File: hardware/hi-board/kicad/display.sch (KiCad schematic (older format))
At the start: 2 parts, among them U2 ER-TFT040-2

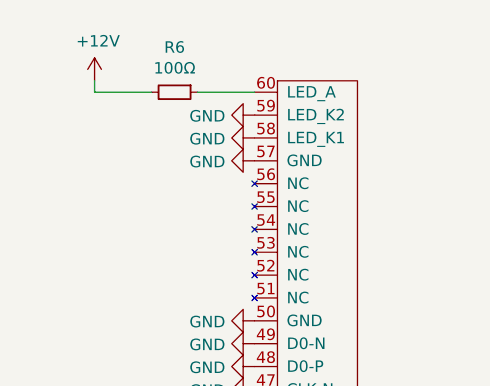
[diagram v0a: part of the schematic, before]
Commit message: Add potentiometer to display schematic
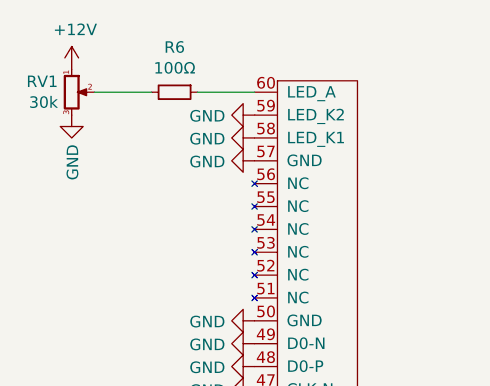
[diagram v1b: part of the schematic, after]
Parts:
- added RV1: 30k, symbol Device:R_POT_Small
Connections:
- net +12V: now also RV1.1; no longer R6.2
- net GND: now also RV1.3
- new net: R6.2, RV1.2
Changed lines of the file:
@@
 Wire Wire Line
 	5750 950  6000 950
-Wire Wire Line
-	5550 950  5300 950
-Wire Wire Line
-	5300 950  5300 900
 $Comp
 L power:+12V #PWR0128
 U 1 1 61427A96
-P 5300 900
-F 0 "#PWR0128" H 5300 750 50  0001 C CNN
-F 1 "+12V" H 5315 1073 50  0000 C CNN
-F 2 "" H 5300 900 50  0001 C CNN
-F 3 "" H 5300 900 50  0001 C CNN
-	1    5300 900
+P 5200 850
+F 0 "#PWR0128" H 5200 700 50  0001 C CNN
+F 1 "+12V" H 5215 1023 50  0000 C CNN
+F 2 "" H 5200 850 50  0001 C CNN
+F 3 "" H 5200 850 50  0001 C CNN
+	1    5200 850
 	1    0    0    -1
 $EndComp
@@
 	0    -1   -1   0
 $EndComp
+$Comp
+L Device:R_POT_Small RV1
+U 1 1 6144926C
+P 5200 950
+F 0 "RV1" H 5140 996 50  0000 R CNN
+F 1 "30k" H 5140 905 50  0000 R CNN
+F 2 "" H 5200 950 50  0001 C CNN
+F 3 "~" H 5200 950 50  0001 C CNN
+	1    5200 950
+	1    0    0    -1
+$EndComp
+$Comp
+L power:GND #PWR0164
+U 1 1 6144A423
+P 5200 1050
+F 0 "#PWR0164" H 5200 800 50  0001 C CNN
+F 1 "GND" V 5205 922 50  0000 R CNN
+F 2 "" H 5200 1050 50  0001 C CNN
+F 3 "" H 5200 1050 50  0001 C CNN
+	1    5200 1050
+	1    0    0    -1
+$EndComp
+Wire Wire Line
+	5300 950  5550 950
 $EndSCHEMATC

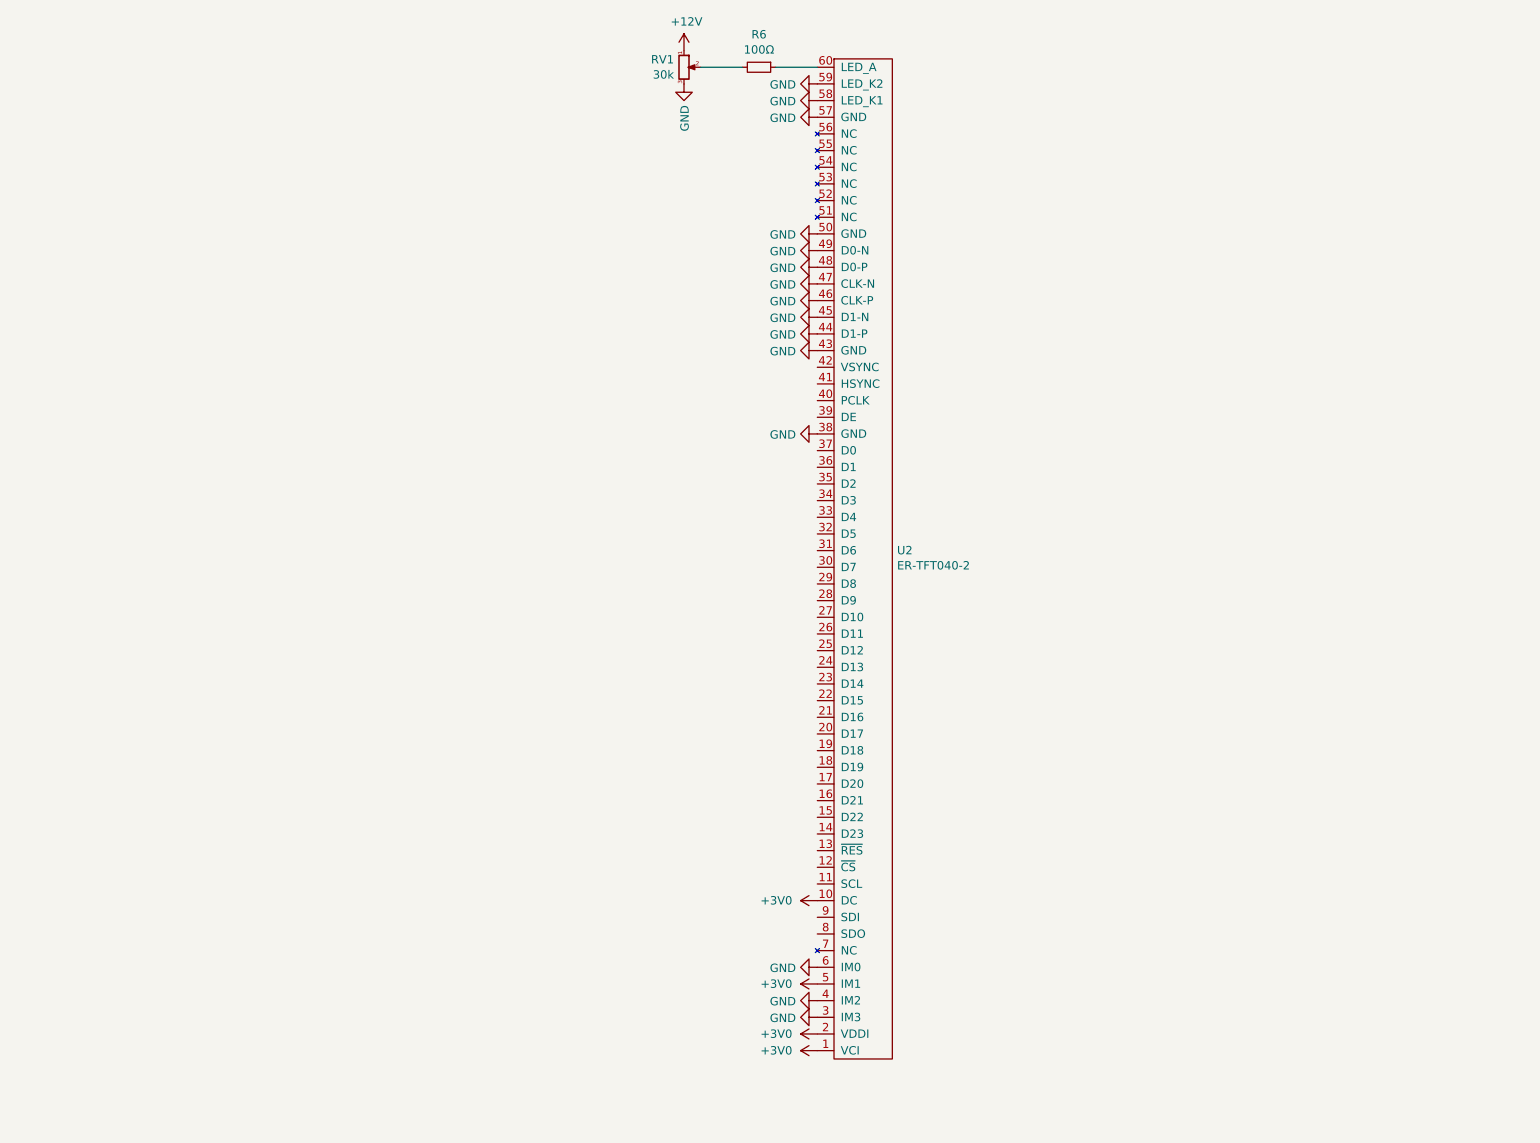
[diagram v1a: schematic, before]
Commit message: Add level shifters
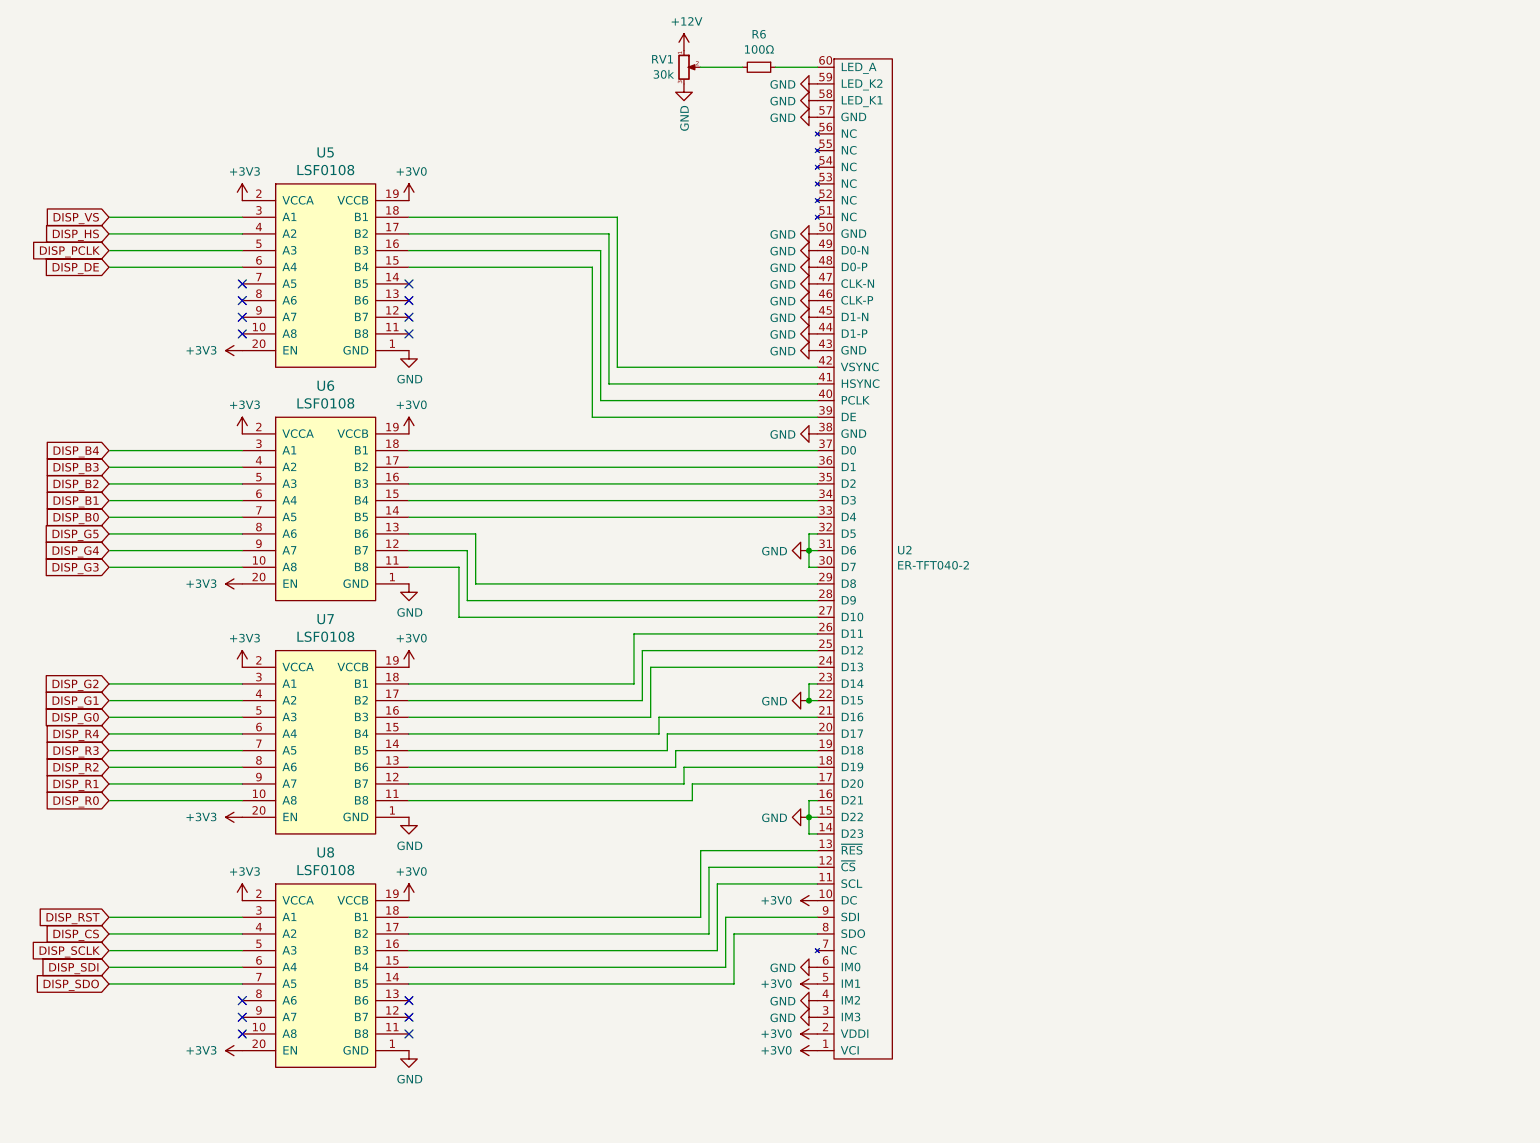
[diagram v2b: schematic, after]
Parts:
- added U5, U6, U7, U8: LSF0108, Package_SO:TSSOP-20_4.4x6.5mm_P0.65mm, symbol hi-board:LSF0108
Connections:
- net +3V0: now also U5.19 (VCCB), U6.19 (VCCB), U7.19 (VCCB), U8.19 (VCCB)
- net GND: now also U2.14 (D23), U2.15 (D22), U2.16 (D21), U2.22 (D15), U2.23 (D14), U2.30 (D7), U2.31 (D6), U2.32 (D5), U5.1 (GND), U6.1 (GND), U7.1 (GND), U8.1 (GND)
- net at U2.11 (SCL): now also U8.16 (B3)
- net at U2.12 (~CS): now also U8.17 (B2)
- net at U2.13 (~RES): now also U8.18 (B1)
- net at U2.17 (D20): now also U7.11 (B8)
- net at U2.18 (D19): now also U7.12 (B7)
- net at U2.19 (D18): now also U7.13 (B6)
- net at U2.20 (D17): now also U7.14 (B5)
- net at U2.21 (D16): now also U7.15 (B4)
- net at U2.24 (D13): now also U7.16 (B3)
- net at U2.25 (D12): now also U7.17 (B2)
- net at U2.26 (D11): now also U7.18 (B1)
- net at U2.27 (D10): now also U6.11 (B8)
- net at U2.28 (D9): now also U6.12 (B7)
- net at U2.29 (D8): now also U6.13 (B6)
- net at U2.33 (D4): now also U6.14 (B5)
- net at U2.34 (D3): now also U6.15 (B4)
- net at U2.35 (D2): now also U6.16 (B3)
- net at U2.36 (D1): now also U6.17 (B2)
- net at U2.37 (D0): now also U6.18 (B1)
- net at U2.39 (DE): now also U5.15 (B4)
- net at U2.40 (PCLK): now also U5.16 (B3)
- net at U2.41 (HSYNC): now also U5.17 (B2)
- net at U2.42 (VSYNC): now also U5.18 (B1)
- net at U2.8 (SDO): now also U8.14 (B5)
- net at U2.9 (SDI): now also U8.15 (B4)
- new net +3V3: U5.2 (VCCA), U5.20 (EN), U6.2 (VCCA), U6.20 (EN), U7.2 (VCCA), U7.20 (EN), U8.2 (VCCA), U8.20 (EN)
- new net DISP_B0: U6.7 (A5)
- new net DISP_B1: U6.6 (A4)
- new net DISP_B2: U6.5 (A3)
- new net DISP_B3: U6.4 (A2)
- new net DISP_B4: U6.3 (A1)
- new net DISP_CS: U8.4 (A2)
- new net DISP_DE: U5.6 (A4)
- new net DISP_G0: U7.5 (A3)
- new net DISP_G1: U7.4 (A2)
- new net DISP_G2: U7.3 (A1)
- new net DISP_G3: U6.10 (A8)
- new net DISP_G4: U6.9 (A7)
- new net DISP_G5: U6.8 (A6)
- new net DISP_HS: U5.4 (A2)
- new net DISP_PCLK: U5.5 (A3)
- new net DISP_R0: U7.10 (A8)
- new net DISP_R1: U7.9 (A7)
- new net DISP_R2: U7.8 (A6)
- new net DISP_R3: U7.7 (A5)
- new net DISP_R4: U7.6 (A4)
- new net DISP_RST: U8.3 (A1)
- new net DISP_SCLK: U8.5 (A3)
- new net DISP_SDI: U8.6 (A4)
- new net DISP_SDO: U8.7 (A5)
- new net DISP_VS: U5.3 (A1)
- no-connect marks 0 -> 14

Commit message: Complete display schematic and change footprints
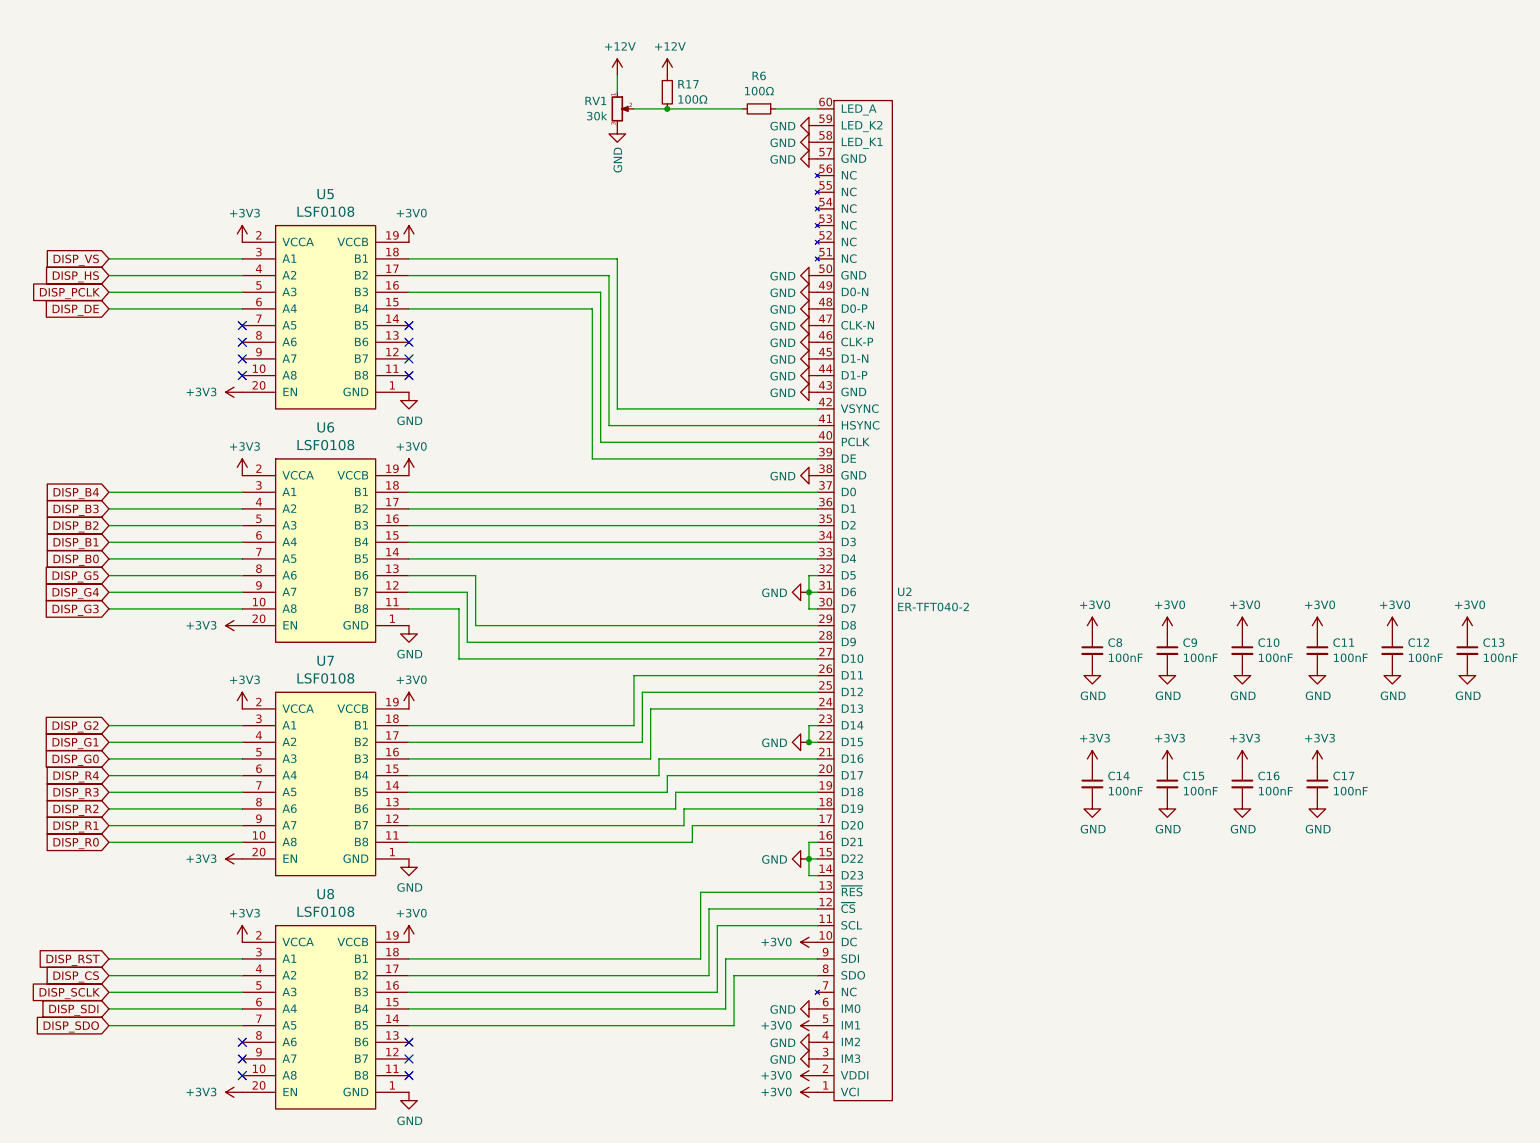
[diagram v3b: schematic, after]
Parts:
- added C10, C11, C12, C13, C14, C15, C16, C17, C8, C9: 100nF, Capacitor_SMD:C_0603_1608Metric, symbol Device:C_Small
- added R17: 100Ω, Resistor_SMD:R_0603_1608Metric, symbol Device:R_Small
- R6: footprint Resistor_SMD:R_0402_1005Metric -> Resistor_SMD:R_0603_1608Metric
- RV1: footprint (none) -> hi-board:Dual_Pot
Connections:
- net +12V: now also R17.1
- net +3V0: now also C10.1, C11.1, C12.1, C13.1, C8.1, C9.1
- net +3V3: now also C14.1, C15.1, C16.1, C17.1
- net GND: now also C10.2, C11.2, C12.2, C13.2, C14.2, C15.2, C16.2, C17.2, C8.2, C9.2
- net at R6.2, RV1.2: now also R17.2
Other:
- moved on the sheet: R6, RV1, U2, U5, U6, U7, U8

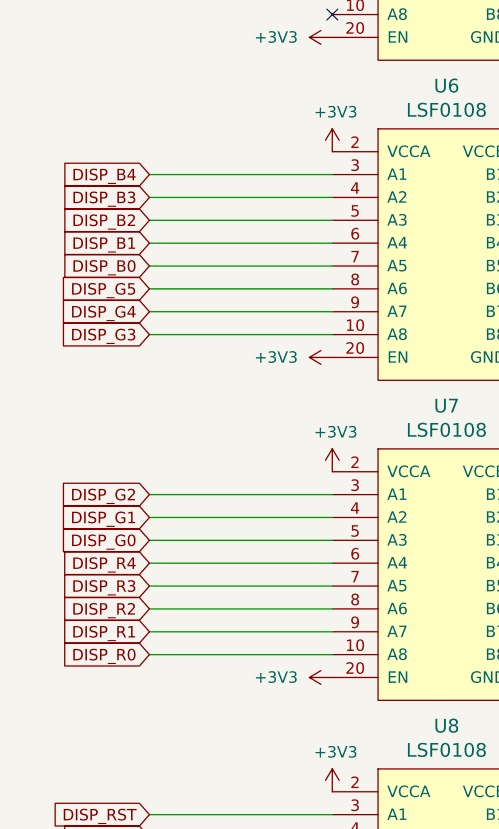
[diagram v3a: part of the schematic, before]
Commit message: Place connector components
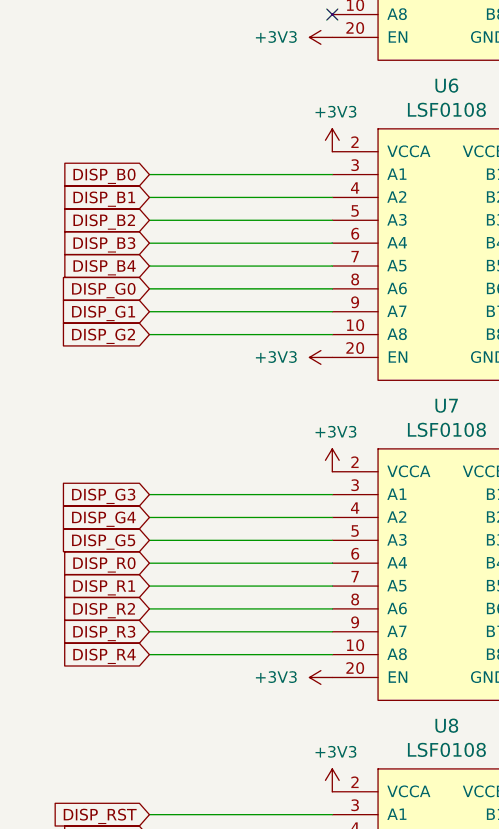
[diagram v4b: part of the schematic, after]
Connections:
- net DISP_B0: now also U6.3 (A1); no longer U6.7 (A5)
- net DISP_B1: now also U6.4 (A2); no longer U6.6 (A4)
- net DISP_B3: now also U6.6 (A4); no longer U6.4 (A2)
- net DISP_B4: now also U6.7 (A5); no longer U6.3 (A1)
- net DISP_G0: now also U6.8 (A6); no longer U7.5 (A3)
- net DISP_G1: now also U6.9 (A7); no longer U7.4 (A2)
- net DISP_G2: now also U6.10 (A8); no longer U7.3 (A1)
- net DISP_G3: now also U7.3 (A1); no longer U6.10 (A8)
- net DISP_G4: now also U7.4 (A2); no longer U6.9 (A7)
- net DISP_G5: now also U7.5 (A3); no longer U6.8 (A6)
- net DISP_R0: now also U7.6 (A4); no longer U7.10 (A8)
- net DISP_R1: now also U7.7 (A5); no longer U7.9 (A7)
- net DISP_R3: now also U7.9 (A7); no longer U7.7 (A5)
- net DISP_R4: now also U7.10 (A8); no longer U7.6 (A4)
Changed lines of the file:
@@
 Wire Wire Line
 	1750 3500 2550 3500
-Text GLabel 1750 5600 0    50   Input ~ 0
+Text GLabel 1750 5200 0    50   Input ~ 0
 DISP_R0
 Wire Wire Line
 	1750 5600 2550 5600
-Text GLabel 1750 5500 0    50   Input ~ 0
+Text GLabel 1750 5300 0    50   Input ~ 0
 DISP_R1
 Text GLabel 1750 5400 0    50   Input ~ 0
 DISP_R2
-Text GLabel 1750 5300 0    50   Input ~ 0
+Text GLabel 1750 5500 0    50   Input ~ 0
 DISP_R3
-Text GLabel 1750 5200 0    50   Input ~ 0
+Text GLabel 1750 5600 0    50   Input ~ 0
 DISP_R4
-Text GLabel 1750 5100 0    50   Input ~ 0
+Text GLabel 1750 4000 0    50   Input ~ 0
 DISP_G0
-Text GLabel 1750 5000 0    50   Input ~ 0
+Text GLabel 1750 4100 0    50   Input ~ 0
 DISP_G1
-Text GLabel 1750 4900 0    50   Input ~ 0
+Text GLabel 1750 4200 0    50   Input ~ 0
 DISP_G2
 Wire Wire Line
@@
 Wire Wire Line
 	3950 4000 3550 4000
-Text GLabel 1750 4200 0    50   Input ~ 0
+Text GLabel 1750 4900 0    50   Input ~ 0
 DISP_G3
 Wire Wire Line
 	1750 4200 2550 4200
-Text GLabel 1750 4100 0    50   Input ~ 0
+Text GLabel 1750 5000 0    50   Input ~ 0
 DISP_G4
-Text GLabel 1750 4000 0    50   Input ~ 0
+Text GLabel 1750 5100 0    50   Input ~ 0
 DISP_G5
 Wire Wire Line
@@
 Wire Wire Line
 	3550 3600 6000 3600
-Text GLabel 1750 3900 0    50   Input ~ 0
+Text GLabel 1750 3500 0    50   Input ~ 0
 DISP_B0
 Wire Wire Line
 	1750 3900 2550 3900
-Text GLabel 1750 3800 0    50   Input ~ 0
+Text GLabel 1750 3600 0    50   Input ~ 0
 DISP_B1
 Text GLabel 1750 3700 0    50   Input ~ 0
 DISP_B2
-Text GLabel 1750 3600 0    50   Input ~ 0
+Text GLabel 1750 3800 0    50   Input ~ 0
 DISP_B3
-Text GLabel 1750 3500 0    50   Input ~ 0
+Text GLabel 1750 3900 0    50   Input ~ 0
 DISP_B4
 Wire Wire Line
